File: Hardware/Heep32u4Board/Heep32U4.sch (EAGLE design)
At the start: 11 parts, among them J2 AVR_SPI_PROG_3X2PTH, U1 ENC28J60-SO, Y1 16MHz

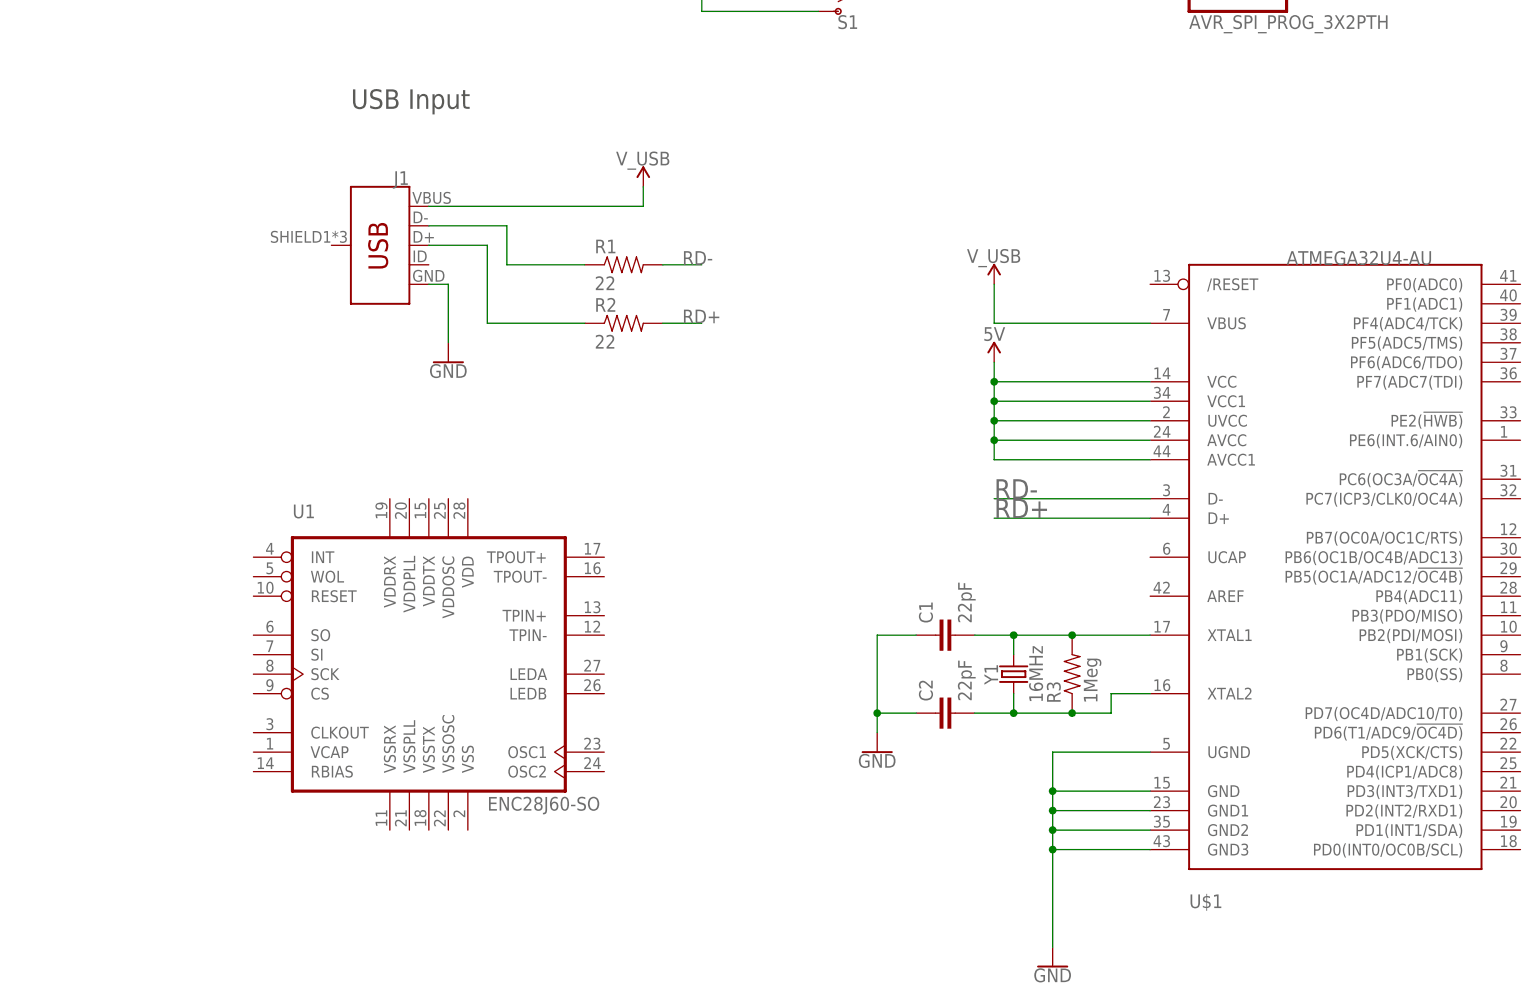
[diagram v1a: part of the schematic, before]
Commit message: #20 Added further labeling
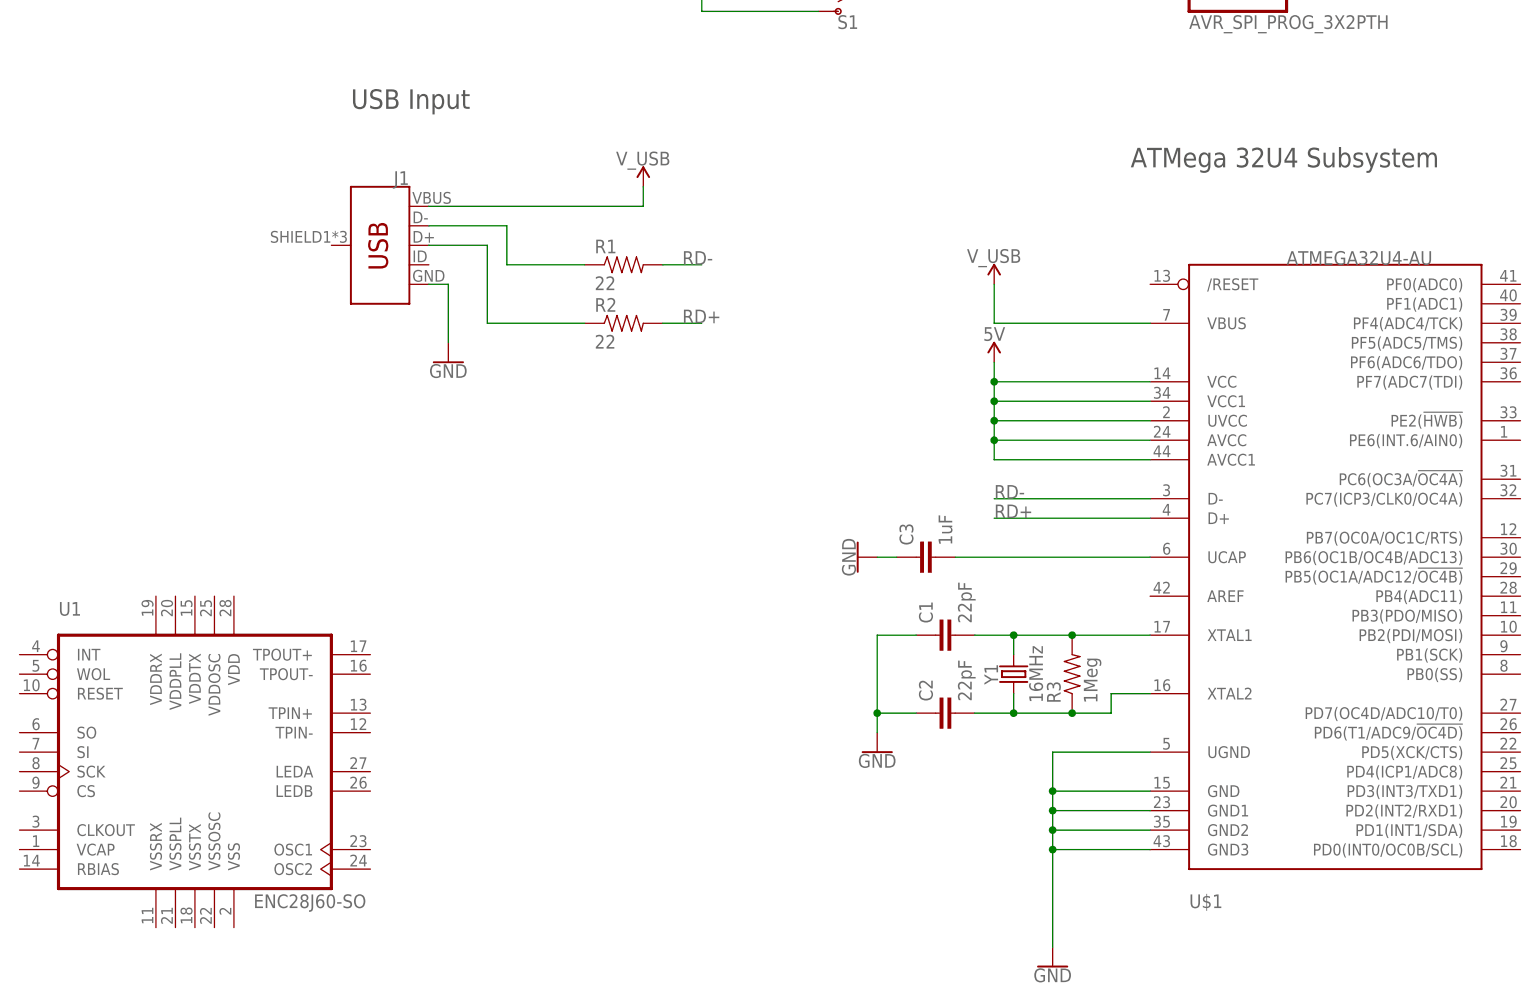
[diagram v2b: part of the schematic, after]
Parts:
- added C3: 1uF, SparkFun-Passives:CAP0603-CAP
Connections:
- new net N$1: C3.2, U$1.UCAP
- net GND: now also C3.1
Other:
- note added: "ATMega 32U4 Subsystem"
- moved on the sheet: U1
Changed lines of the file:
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@@
 <part name="GND2" library="SparkFun-PowerSymbols" deviceset="GND" device=""/>
 <part name="GND3" library="SparkFun-PowerSymbols" deviceset="GND" device=""/>
+<part name="C3" library="SparkFun-Passives" deviceset="CAP" device="0603-CAP" value="1uF"/>
+<part name="GND4" library="SparkFun-PowerSymbols" deviceset="GND" device=""/>
 </parts>
 <sheets>
@@
 <text x="-20.32" y="109.22" size="2.54" layer="97">USB Input</text>
 <text x="22.86" y="139.7" size="2.54" layer="97">Primary Power Switch</text>
+<text x="81.28" y="101.6" size="2.54" layer="97">ATMega 32U4 Subsystem</text>
 </plain>
 <instances>
 <instance part="U$1" gate="G$1" x="106.68" y="43.18"/>
-<instance part="U1" gate="G$1" x="-7.62" y="33.02"/>
+<instance part="U1" gate="G$1" x="-38.1" y="20.32"/>
 <instance part="J1" gate="G$1" x="-15.24" y="91.44" rot="MR0"/>
 <instance part="Y1" gate="G$1" x="66.04" y="35.56" rot="R90"/>
@@
 <instance part="GND2" gate="1" x="48.26" y="25.4"/>
 <instance part="GND3" gate="1" x="71.12" y="-2.54"/>
+<instance part="C3" gate="G$1" x="55.88" y="50.8" rot="R90"/>
+<instance part="GND4" gate="1" x="45.72" y="50.8" rot="R270"/>
 </instances>
 <busses>
@@
 <pinref part="U$1" gate="G$1" pin="D-"/>
 <wire x1="83.82" y1="58.42" x2="63.5" y2="58.42" width="0.1524" layer="91"/>
-<label x="63.5" y="58.42" size="2.54" layer="95"/>
+<label x="63.5" y="58.42" size="1.778" layer="95"/>
 </segment>
 </net>
@@
 <pinref part="U$1" gate="G$1" pin="D+"/>
 <wire x1="83.82" y1="55.88" x2="63.5" y2="55.88" width="0.1524" layer="91"/>
-<label x="63.5" y="55.88" size="2.54" layer="95"/>
+<label x="63.5" y="55.88" size="1.778" layer="95"/>
 </segment>
 </net>
@@
 <pinref part="GND3" gate="1" pin="GND"/>
 </segment>
+<segment>
+<pinref part="C3" gate="G$1" pin="1"/>
+<pinref part="GND4" gate="1" pin="GND"/>
+<wire x1="50.8" y1="50.8" x2="48.26" y2="50.8" width="0.1524" layer="91"/>
+</segment>
 </net>
 <net name="5V" class="0">
@@
 </segment>
 </net>
+<net name="N$1" class="0">
+<segment>
+<pinref part="U$1" gate="G$1" pin="UCAP"/>
+<pinref part="C3" gate="G$1" pin="2"/>
+<wire x1="83.82" y1="50.8" x2="58.42" y2="50.8" width="0.1524" layer="91"/>
+</segment>
+</net>

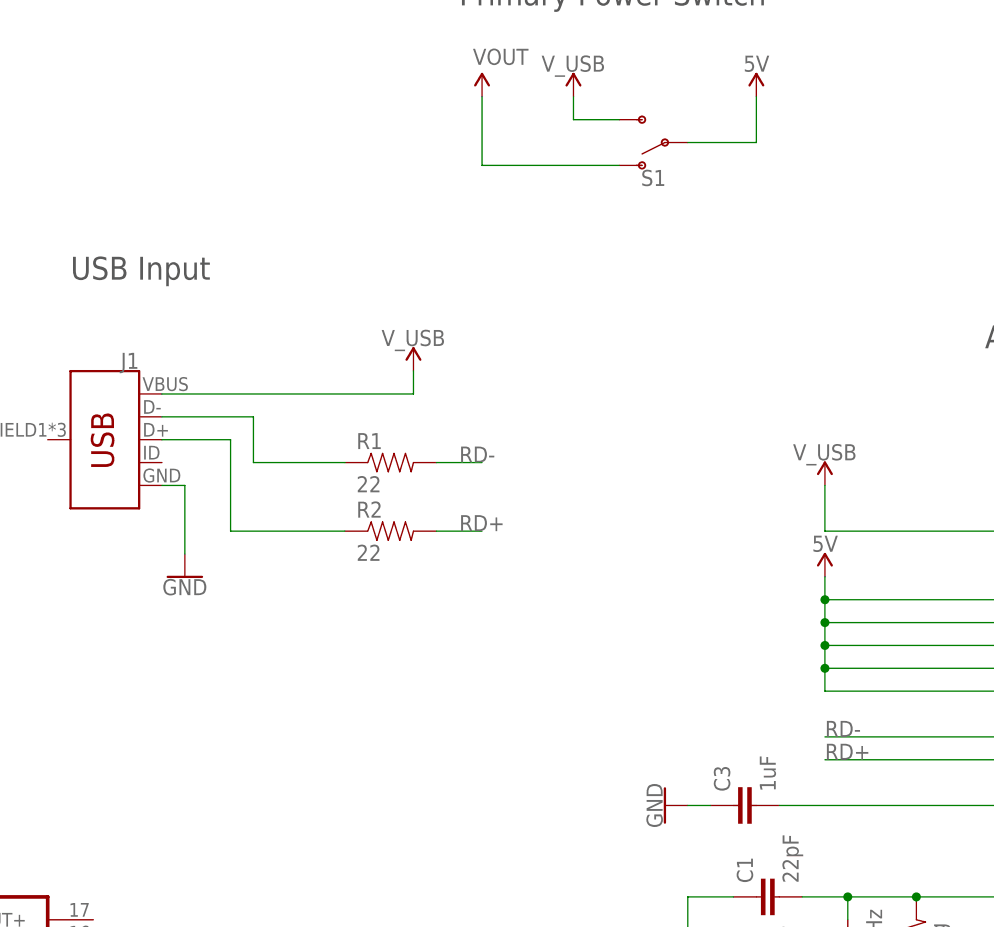
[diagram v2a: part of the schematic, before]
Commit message: #20 Added more filtering to the VCC line of 32U4
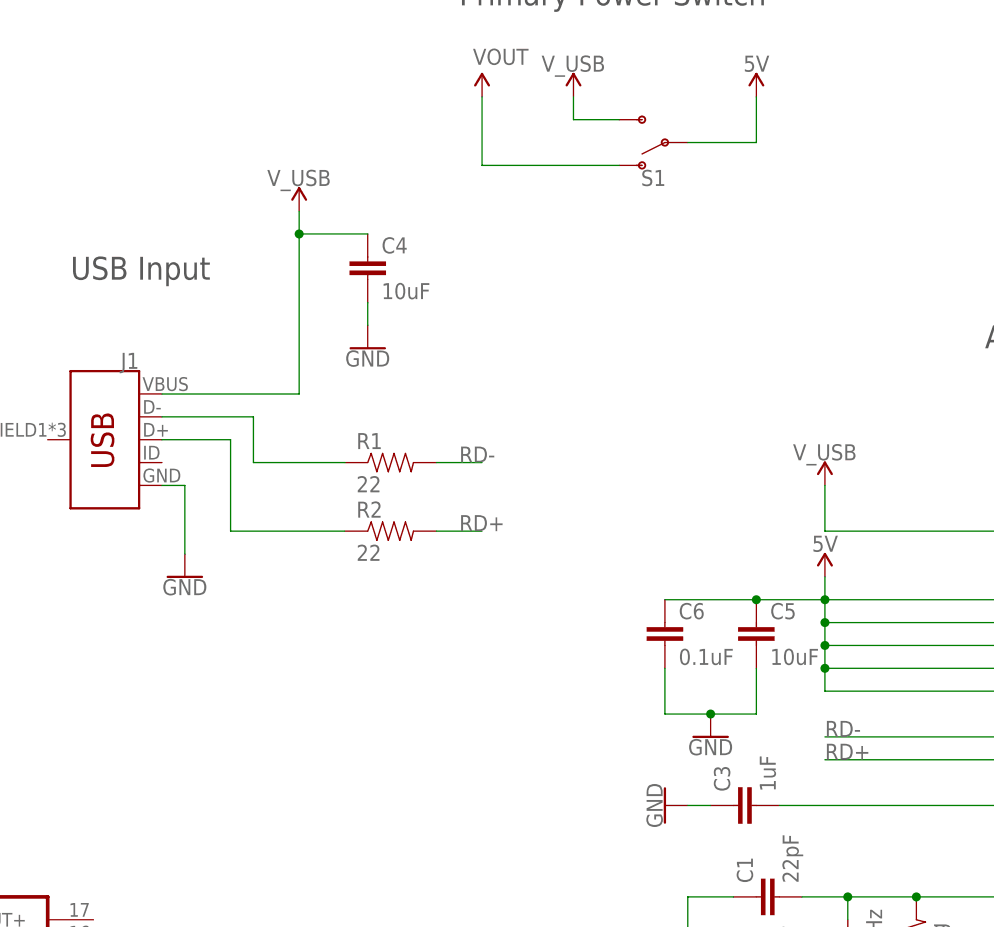
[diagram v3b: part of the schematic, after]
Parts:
- added C4, C5: 10uF, SparkFun-Passives:CAP0603-CAP
- added C6: 0.1uF, SparkFun-Passives:CAP0603-CAP
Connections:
- net 5V: now also C5.1, C6.1
- net GND: now also C4.2, C5.2, C6.2
- net V_USB: now also C4.1
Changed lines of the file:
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@@
 <part name="C3" library="SparkFun-Passives" deviceset="CAP" device="0603-CAP" value="1uF"/>
 <part name="GND4" library="SparkFun-PowerSymbols" deviceset="GND" device=""/>
+<part name="C4" library="SparkFun-Passives" deviceset="CAP" device="0603-CAP" value="10uF"/>
+<part name="GND5" library="SparkFun-PowerSymbols" deviceset="GND" device=""/>
+<part name="C5" library="SparkFun-Passives" deviceset="CAP" device="0603-CAP" value="10uF"/>
+<part name="C6" library="SparkFun-Passives" deviceset="CAP" device="0603-CAP" value="0.1uF"/>
+<part name="GND6" library="SparkFun-PowerSymbols" deviceset="GND" device=""/>
 </parts>
 <sheets>
@@
 <instance part="R1" gate="G$1" x="15.24" y="88.9"/>
 <instance part="R2" gate="G$1" x="15.24" y="81.28"/>
-<instance part="SUPPLY1" gate="G$1" x="17.78" y="99.06"/>
+<instance part="SUPPLY1" gate="G$1" x="5.08" y="116.84"/>
 <instance part="GND1" gate="1" x="-7.62" y="76.2"/>
 <instance part="SUPPLY2" gate="G$1" x="63.5" y="86.36"/>
@@
 <instance part="C3" gate="G$1" x="55.88" y="50.8" rot="R90"/>
 <instance part="GND4" gate="1" x="45.72" y="50.8" rot="R270"/>
+<instance part="C4" gate="G$1" x="12.7" y="109.22"/>
+<instance part="GND5" gate="1" x="12.7" y="101.6"/>
+<instance part="C5" gate="G$1" x="55.88" y="68.58"/>
+<instance part="C6" gate="G$1" x="45.72" y="68.58"/>
+<instance part="GND6" gate="1" x="50.8" y="58.42"/>
 </instances>
 <busses>
@@
 <net name="V_USB" class="0">
 <segment>
-<wire x1="17.78" y1="96.52" x2="17.78" y2="99.06" width="0.1524" layer="91"/>
+<wire x1="5.08" y1="96.52" x2="5.08" y2="114.3" width="0.1524" layer="91"/>
 <pinref part="SUPPLY1" gate="G$1" pin="V_USB"/>
 <pinref part="J1" gate="G$1" pin="VBUS"/>
-<wire x1="-10.16" y1="96.52" x2="17.78" y2="96.52" width="0.1524" layer="91"/>
+<wire x1="5.08" y1="114.3" x2="5.08" y2="116.84" width="0.1524" layer="91"/>
+<wire x1="-10.16" y1="96.52" x2="5.08" y2="96.52" width="0.1524" layer="91"/>
+<pinref part="C4" gate="G$1" pin="1"/>
+<wire x1="5.08" y1="114.3" x2="12.7" y2="114.3" width="0.1524" layer="91"/>
+<junction x="5.08" y="114.3"/>
 </segment>
 <segment>
@@
 <wire x1="50.8" y1="50.8" x2="48.26" y2="50.8" width="0.1524" layer="91"/>
 </segment>
+<segment>
+<pinref part="C4" gate="G$1" pin="2"/>
+<pinref part="GND5" gate="1" pin="GND"/>
+<wire x1="12.7" y1="106.68" x2="12.7" y2="104.14" width="0.1524" layer="91"/>
+</segment>
+<segment>
+<pinref part="C6" gate="G$1" pin="2"/>
+<wire x1="45.72" y1="66.04" x2="45.72" y2="60.96" width="0.1524" layer="91"/>
+<pinref part="C5" gate="G$1" pin="2"/>
+<wire x1="45.72" y1="60.96" x2="50.8" y2="60.96" width="0.1524" layer="91"/>
+<wire x1="50.8" y1="60.96" x2="55.88" y2="60.96" width="0.1524" layer="91"/>
+<wire x1="55.88" y1="60.96" x2="55.88" y2="66.04" width="0.1524" layer="91"/>
+<pinref part="GND6" gate="1" pin="GND"/>
+<junction x="50.8" y="60.96"/>
+</segment>
 </net>
 <net name="5V" class="0">
@@
 <junction x="63.5" y="73.66"/>
 <pinref part="SUPPLY6" gate="G$1" pin="5V"/>
-</segment>
-</net>
+<pinref part="C5" gate="G$1" pin="1"/>
+<wire x1="63.5" y1="73.66" x2="55.88" y2="73.66" width="0.1524" layer="91"/>
+<pinref part="C6" gate="G$1" pin="1"/>
+<wire x1="55.88" y1="73.66" x2="45.72" y2="73.66" width="0.1524" layer="91"/>
+<junction x="55.88" y="73.66"/>
+</segment>
+</net>

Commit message: Changed board to use 3v instead of 5v due to ENC28J60 constraints
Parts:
- added C10, C9: 10pF, SparkFun-Passives:CAP0603-CAP
- added C11, C12, C13, C14, C15, C7, C8: 0.1uF, SparkFun-Capacitors:CAP0603-CAP
- added C16, C18, C20: 10uF, SparkFun-Passives:CAP0603-CAP
- added C17, C19: 100nF, SparkFun-Passives:CAP0603-CAP
- added J4: MAGJACK, SparkFun-Connectors:MAGJACK
- added L1: (no value), SparkFun-Passives:INDUCTOR0603
- added Q1: 25MHz, adafruit:CRYSTALSM49
- added R10: 2k @ 1% Tolerance, SparkFun-Passives:RESISTOR0603-RES
- added R4, R5, R6, R7: 51, SparkFun-Resistors:RESISTOR0603
- added R8, R9: 200, SparkFun-Resistors:RESISTOR0603
- added S2: MOMENTARY-SWITCH-SPST-PTH-6.0MM, SparkFun-Switches:MOMENTARY-SWITCH-SPST-PTH-6.0MM
- added U2: ENC28J60-SO, microchip-enc28j60:ENC28J60-SO
- U1: value ENC28J60-SO -> +3.3v; device microchip-enc28j60:ENC28J60-SO -> SparkFun-IC-Power:V_REG_78XX7812
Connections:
- new net #CS: U2.CS
- new net #RESET: U2.RESET
- new net 3.3V: C11.1, C12.1, C13.1, C14.1, C15.1, C19.1, C20.1, C5.1, C6.1, L1.1, U$1.AVCC, U$1.AVCC1, U$1.UVCC, U$1.VCC, U$1.VCC1, U1.OUT, U2.VDD, U2.VDDOSC, U2.VDDPLL, U2.VDDRX, U2.VDDTX
- new net CS: U$1.PB6(OC1B/OC4B/ADC13)
- new net LEDA: J4.GLED+, U2.LEDA
- new net LEDB: J4.YLED+, U2.LEDB
- new net N$11: C7.1, J4.TCT, L1.2, R4.1, R5.1
- new net N$12: J4.YLED-, R9.2
- new net N$13: J4.GLED-, R8.2
- new net N$14: C9.1, Q1.2, U2.OSC1
- new net N$15: C10.1, Q1.1, U2.OSC2
- new net N$16: R10.1, U2.RBIAS
- new net N$17: C16.2, U2.VCAP
- new net N$2: J4.RD+, R6.2, U2.TPIN+
- new net N$5: J4.RD-, R7.2, U2.TPIN-
- new net N$6: J4.TD-, R4.2, U2.TPOUT-
- new net N$7: J4.TD+, R5.2, U2.TPOUT+
- new net N$8: C8.1, R6.1, R7.1
- new net RESET: J2.5, S2.2, U$1./RESET
- new net SCK: J2.3, U$1.PB1(SCK), U2.SCK
- new net SI: J2.4, U$1.PB2(PDI/MOSI), U2.SI
- new net SO: J2.1, U$1.PB3(PDO/MISO), U2.SO
- new net VIN: S1.O
- net 5V: now also J2.2; no longer C5.1, C6.1, S1.P, U$1.AVCC, U$1.AVCC1, U$1.UVCC, U$1.VCC, U$1.VCC1
- net GND: now also C10.2, C11.2, C12.2, C13.2, C14.2, C15.2, C16.1, C17.2, C18.2, C19.2, C20.2, C7.2, C8.2, C9.2, J2.6, J4.SHIELD@0, J4.SHIELD@1, R10.2, R8.1, R9.1, S2.1, U1.GND, U2.VSS, U2.VSSOSC, U2.VSSPLL, U2.VSSRX, U2.VSSTX
- net VOUT: now also C17.1, C18.1, S1.P, U1.IN; no longer S1.O
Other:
- note added: "AVR Programmer"
- note added: "ENC28J60 and RJ45 Subsystem"
- moved on the sheet: J2, S1

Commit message: #20 First layout steps
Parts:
- added J3: (no value), SparkFun-Connectors:CONN_02
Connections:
- net GND: now also J3.2
- net VIN: now also J3.1
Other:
- note added: "Voltage Regulator (LDO)"
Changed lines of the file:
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@@
 <part name="SUPPLY12" library="SparkFun-PowerSymbols" deviceset="VOUT" device=""/>
 <part name="SUPPLY6" library="SparkFun-Aesthetics" deviceset="3.3V" device=""/>
+<part name="J3" library="SparkFun-Connectors" deviceset="CONN_02" device=""/>
+<part name="SUPPLY11" library="SparkFun-PowerSymbols" deviceset="VIN" device=""/>
+<part name="GND19" library="SparkFun-Aesthetics" deviceset="GND" device=""/>
 </parts>
 <sheets>
@@
 <text x="99.06" y="167.64" size="2.54" layer="97">AVR Programmer</text>
 <text x="-185.42" y="187.96" size="5.08" layer="97">ENC28J60 and RJ45 Subsystem</text>
+<text x="-83.82" y="60.96" size="2.54" layer="97">Voltage Regulator (LDO)</text>
 </plain>
 <instances>
@@
 <instance part="SUPPLY12" gate="G$1" x="-88.9" y="48.26"/>
 <instance part="SUPPLY6" gate="G$1" x="63.5" y="76.2"/>
+<instance part="J3" gate="G$1" x="-50.8" y="185.42" rot="MR180"/>
+<instance part="SUPPLY11" gate="G$1" x="-35.56" y="193.04"/>
+<instance part="GND19" gate="1" x="-35.56" y="175.26"/>
 </instances>
 <busses>
@@
 <wire x1="-83.82" y1="27.94" x2="-76.2" y2="27.94" width="0.1524" layer="91"/>
 <junction x="-76.2" y="27.94"/>
+</segment>
+<segment>
+<pinref part="J3" gate="G$1" pin="2"/>
+<wire x1="-43.18" y1="182.88" x2="-35.56" y2="182.88" width="0.1524" layer="91"/>
+<wire x1="-35.56" y1="182.88" x2="-35.56" y2="177.8" width="0.1524" layer="91"/>
+<pinref part="GND19" gate="1" pin="GND"/>
 </segment>
 </net>
@@
 <pinref part="SUPPLY4" gate="G$1" pin="VIN"/>
 </segment>
-</net>
+<segment>
+<pinref part="J3" gate="G$1" pin="1"/>
+<wire x1="-43.18" y1="185.42" x2="-35.56" y2="185.42" width="0.1524" layer="91"/>
+<wire x1="-35.56" y1="185.42" x2="-35.56" y2="193.04" width="0.1524" layer="91"/>
+<pinref part="SUPPLY11" gate="G$1" pin="VIN"/>
+</segment>
+</net>

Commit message: #20 Added relays to 32u4 schematic
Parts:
- added D1, D2: 200mA/100V/1V, SparkFun-DiscreteSemi:DIODE-1N4148
- added D3, D4: RED, SparkFun-LED:LED-RED0603
- added D5: GREEN, SparkFun-LED:LED-GREEN0603
- added J5, J6: (no value), SparkFun-Connectors:CONN_025MM
- added J7: (no value), SparkFun-Connectors:CONN_05
- added K1, K2: RELAY-SPDT-JZC-11F, SparkFun-Electromechanical:RELAY-SPDT-JZC-11F
- added Q2, Q3: 5.8A/30V/35mΩ, SparkFun-DiscreteSemi:MOSFET-NCH-AO3404A
- added R11, R12: 100k, SparkFun-Passives:RESISTOR0603-RES
- added R13, R14, R15: 1k, SparkFun-Passives:RESISTOR0603-RES
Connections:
- new net N$18: J5.2, K1.NO
- new net N$19: J5.1, K1.MAIN
- new net N$20: J6.2, K2.NO
- new net N$21: J6.1, K2.MAIN
- new net N$22: D2.A, K2.COIL1, Q3.D
- new net N$23: D1.A, K1.COIL1, Q2.D
- new net N$24: D5.A, R15.1
- new net N$32: D4.A, R14.1
- new net N$33: D3.A, R13.1
- new net RELAY1: Q2.G, R11.2, R13.2, U$1.PD7(OC4D/ADC10/T0)
- new net RELAY2: Q3.G, R12.2, R14.2, U$1.PD6(T1/ADC9/!OC4D)
- net 3.3V: now also J7.2, R15.2
- net GND: now also D3.C, D4.C, D5.C, J7.1, Q2.S, Q3.S, R11.1, R12.1
- net VIN: now also J7.5
- net VOUT: now also D1.C, D2.C, J7.3, K1.COIL2, K2.COIL2
- net V_USB: now also J7.4
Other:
- note added: "Power LED"
- note added: "Relay Corridor"
- note added: "Test Points"
